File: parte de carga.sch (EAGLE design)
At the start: 28 parts, among them IC1 MCP73831T-2ACI_OT, IC10 741G3157DBVR, IC15 LMV321AIDCKR, IC16 LMV321AIDCKR, IC2 ESP32-S3-WROOM-1-N16R8, IC5 LMV321AIDCKR, IC6 LMV321AIDCKR, IC7 AD8226ARZ, IC8 AD8226ARZ, IC9 LP38692MP-3.3_NOPB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

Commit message: Correcciones del profesor
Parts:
- removed C14: SMDTD03220QA00KS00, SMDTD03220QA00KS00:SMDTD03220QA00KS00
- removed IC6: LMV321AIDCKR, LMV321AIDCKR:LMV321AIDCKR
- removed IC8: AD8226ARZ, AD8226ARZ:AD8226ARZ
- removed R17, R19: (no value), resistor-shunt:BVS
- added R5: (no value), rcl:R-EU_R0805
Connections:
- removed net N$16: IC9.OUT, PS1.EN, PS1.VIN
- removed net N$18: IC8.VOUT
- removed net N$23: IC8.-IN
- removed net N$24: IC7.REF, IC8.REF, PS1.VBIAS
- removed net N$26: IC8.+IN
- removed net N$29: C14.1, IC6.OUT, R19.1
- removed net N$52: C14.2, R19.2
- removed net N$53: IC6.-IN, R17.1
- new net +3V3: IC7.+VS, IC9.OUT, PS1.EN, PS1.VIN
- new net +5V: J1.1
- new net N$10: IC7.RG_1, R5.2
- new net N$12: IC7.RG_2, R5.1
- net GND: now also IC7.-VS; no longer IC6.V-
- net N$22: no longer R17.2
- net VCC: no longer IC6.V+, J1.1
- net VSS: now also IC7.REF, PS1.VBIAS; no longer IC6.+IN
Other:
- moved on the sheet: IC9, PS1

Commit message: cambie resistencias y condensadores
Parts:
- removed C12, C9: SMDTD03220QA00KS00, SMDTD03220QA00KS00:SMDTD03220QA00KS00
- removed R15, R16, R28, R29: (no value), resistor-shunt:BVS
- added C10, C11: 0.1uF, capacitor-wima:C2.5/6
- added C4: 10uF, Capacitor:C-POL_TANTALUM-1206(3216-METRIC)
- added C5, C6, C7: (no value), capacitor-wima:C2.5/6
- added R1, R11, R12: 2k, resistor-shunt:BVS
- added R10: 220, resistor-shunt:BVS
- added R6: 3.2k, resistor-shunt:BVS
- added R7: 1k, resistor-shunt:BVS
- added R8: 10k, resistor-shunt:BVS
- added R9: 450, resistor-shunt:BVS
- C8: value SMDTD03220QA00KS00 -> 10uF; device SMDTD03220QA00KS00:SMDTD03220QA00KS00 -> Capacitor:C-POL_TANTALUM-1206(3216-METRIC)
- R14: value (none) -> 1.6k
- R18: value (none) -> 450
- R5: value (none) -> 50
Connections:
- removed net BATT: SL1.1
- removed net N$22: C9.1, IC5.OUT, R16.1
- removed net N$48: C12.2, R15.2
- removed net N$49: C12.1, R28.1
- new net N$13: C6.2, IC16.+IN, R7.1
- net +BATT: now also C8.+
- net GND: now also C10.2, C11.1, C4.-, C8.-, R1.2, SL1.1
- net N$1: now also R10.1
- net N$2: now also R10.2
- net N$3: now also R1.1
- net N$4: now also C10.1, R11.2
- net N$46: now also R6.2; no longer R29.2
- net N$47: now also C6.1, R6.1, R8.2; no longer R29.1
- net N$5: now also R12.2
- net N$6: now also C5.2; no longer C8.2
- net N$7: now also C7.1, IC5.OUT, R9.1; no longer IC16.-IN, IC16.OUT, R15.1, R18.2
- net N$8: now also IC16.-IN, IC16.OUT, R18.2, R8.1; no longer IC16.+IN
- net N$9: now also C7.2, R9.2; no longer C9.2, R16.2
- net VCC: now also C11.2, C4.+, IC5.V+, R11.1, R12.1
- net VSS: now also R7.2; no longer R28.2
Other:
- moved on the sheet: S1

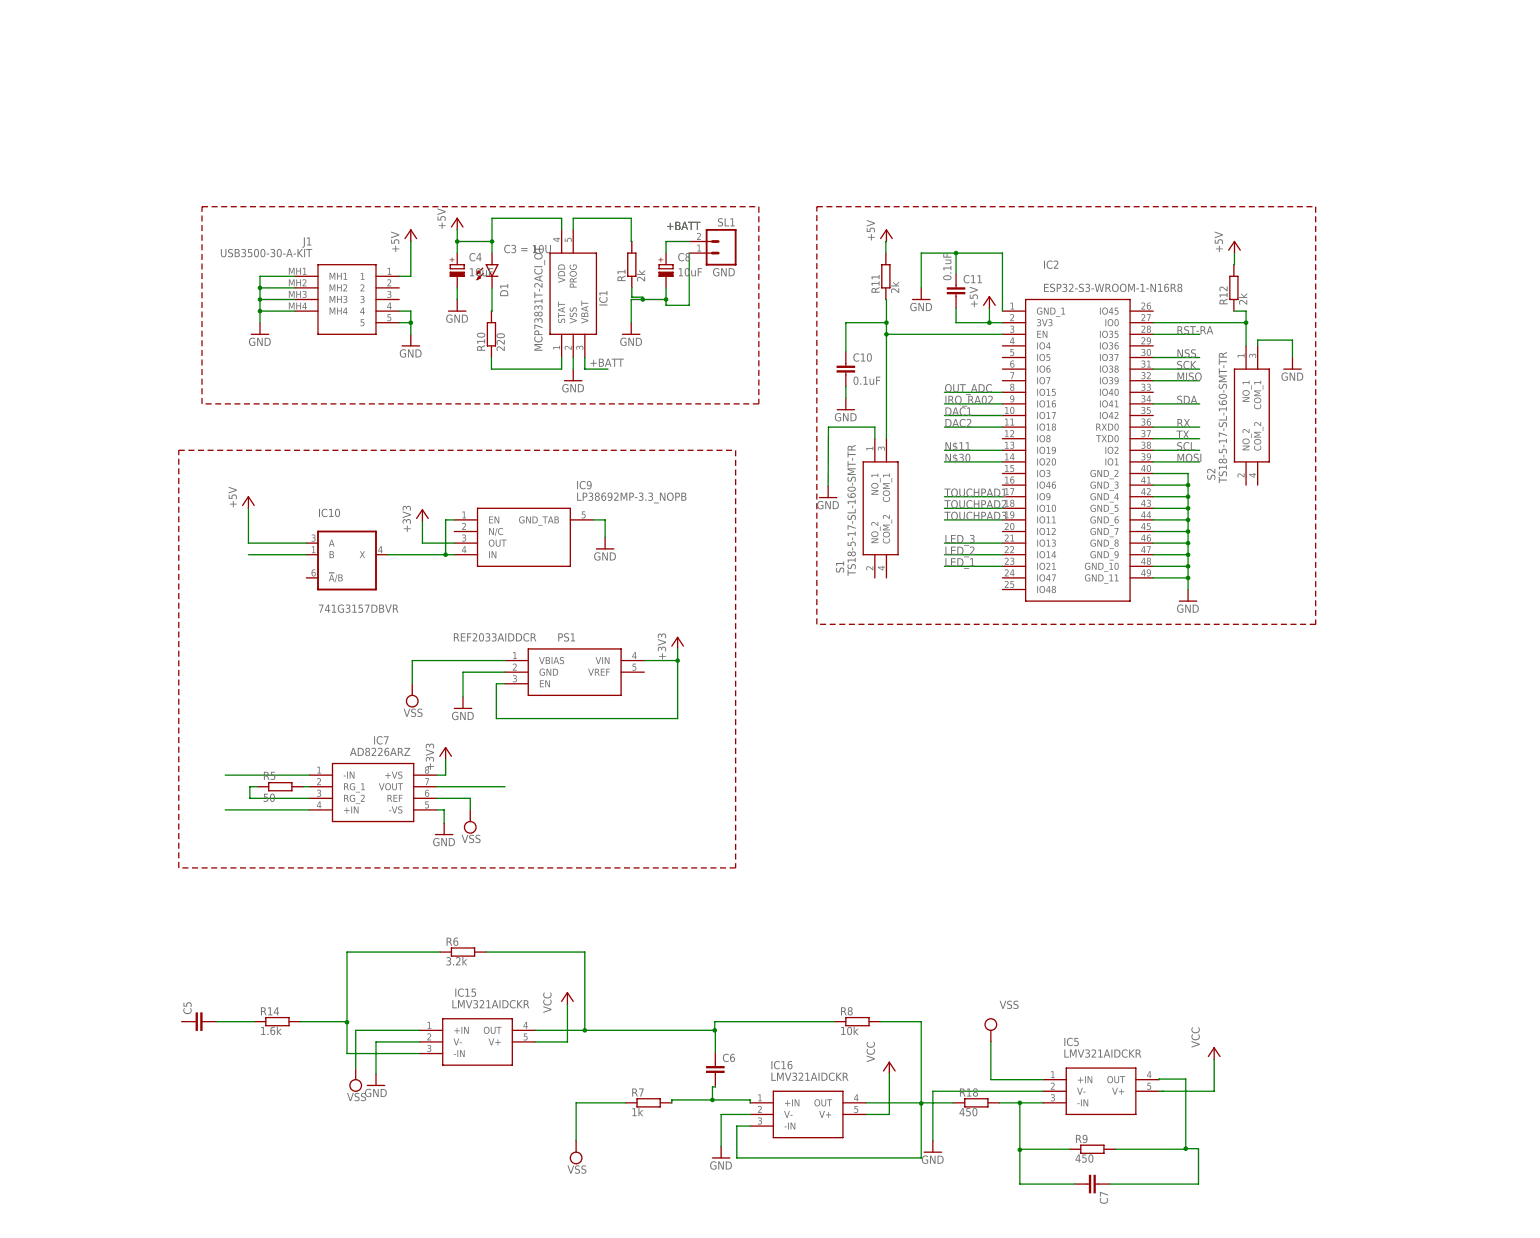
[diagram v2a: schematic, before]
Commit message: Cambie las fuentes y algunos valores a las resistencias
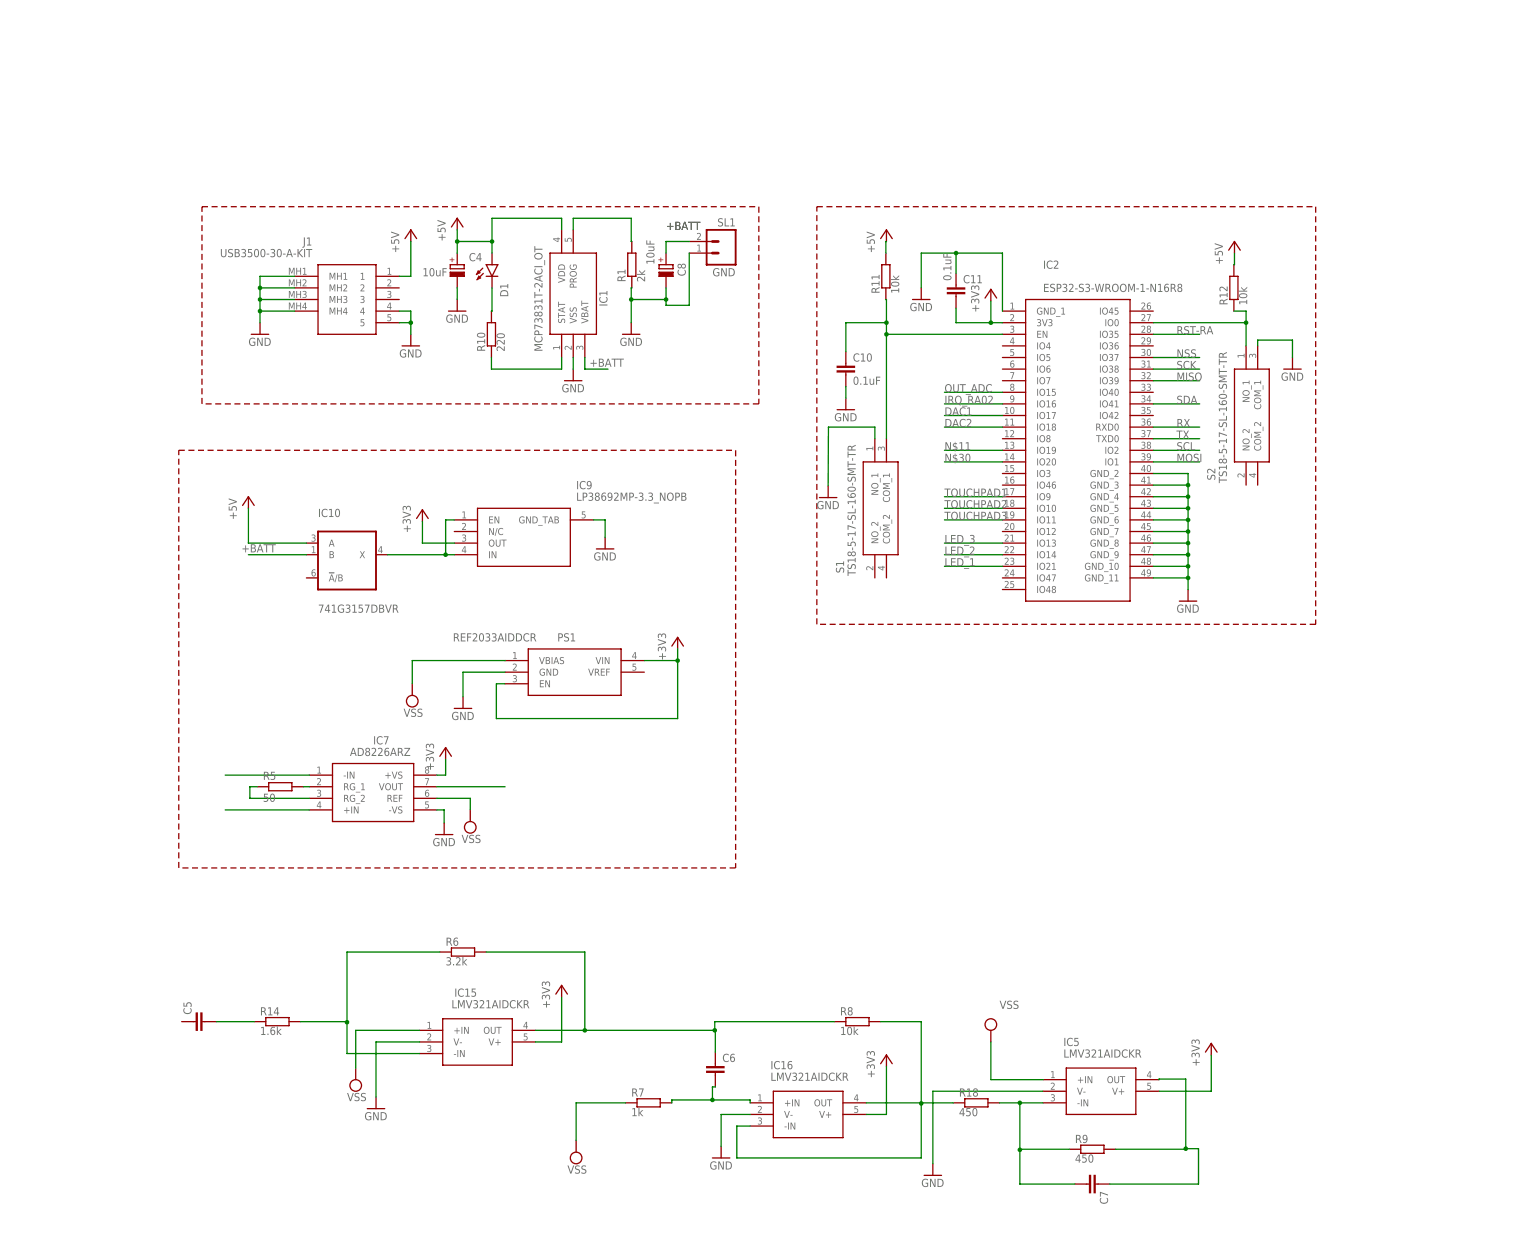
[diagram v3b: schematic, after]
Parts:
- R11, R12: value 2k -> 10k
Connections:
- removed net VCC: C11.2, C4.+, D1.A, IC1.VDD, IC10G$1.A, IC15.V+, IC16.V+, IC2.3V3, IC5.V+, R11.1, R12.1
- net +3V3: now also C11.2, IC15.V+, IC16.V+, IC2.3V3, IC5.V+
- net +5V: now also C4.+, D1.A, IC1.VDD, IC10G$1.A, R11.1, R12.1

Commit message: cambie la escala del esquematico
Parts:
- added R2: (no value), rcl:R-EU_R0805
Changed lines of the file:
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@@
 <setting verticaltext="up"/>
 </settings>
-<grid distance="0.1" unitdist="inch" unit="inch" style="lines" multiple="1" display="no" altdistance="0.01" altunitdist="inch" altunit="inch"/>
+<grid distance="50" unitdist="mil" unit="mil" style="lines" multiple="1" display="no" altdistance="0.01" altunitdist="inch" altunit="inch"/>
 <layers>
-<layer number="1" name="Top" color="4" fill="1" visible="no" active="no"/>
-<layer number="2" name="Route2" color="1" fill="3" visible="no" active="no"/>
-<layer number="3" name="Route3" color="4" fill="3" visible="no" active="no"/>
-<layer number="4" name="Route4" color="1" fill="4" visible="no" active="no"/>
-<layer number="5" name="Route5" color="4" fill="4" visible="no" active="no"/>
-<layer number="6" name="Route6" color="1" fill="8" visible="no" active="no"/>
-<layer number="7" name="Route7" color="4" fill="8" visible="no" active="no"/>
-<layer number="8" name="Route8" color="1" fill="2" visible="no" active="no"/>
-<layer number="9" name="Route9" color="4" fill="2" visible="no" active="no"/>
-<layer number="10" name="Route10" color="1" fill="7" visible="no" active="no"/>
-<layer number="11" name="Route11" color="4" fill="7" visible="no" active="no"/>
-<layer number="12" name="Route12" color="1" fill="5" visible="no" active="no"/>
-<layer number="13" name="Route13" color="4" fill="5" visible="no" active="no"/>
-<layer number="14" name="Route14" color="1" fill="6" visible="no" active="no"/>
-<layer number="15" name="Route15" color="4" fill="6" visible="no" active="no"/>
-<layer number="16" name="Bottom" color="1" fill="1" visible="no" active="no"/>
-<layer number="17" name="Pads" color="2" fill="1" visible="no" active="no"/>
-<layer number="18" name="Vias" color="2" fill="1" visible="no" active="no"/>
-<layer number="19" name="Unrouted" color="6" fill="1" visible="no" active="no"/>
-<layer number="20" name="Dimension" color="15" fill="1" visible="no" active="no"/>
-<layer number="21" name="tPlace" color="7" fill="1" visible="no" active="no"/>
-<layer number="22" name="bPlace" color="7" fill="1" visible="no" active="no"/>
-<layer number="23" name="tOrigins" color="15" fill="1" visible="no" active="no"/>
-<layer number="24" name="bOrigins" color="15" fill="1" visible="no" active="no"/>
-<layer number="25" name="tNames" color="7" fill="1" visible="no" active="no"/>
-<layer number="26" name="bNames" color="7" fill="1" visible="no" active="no"/>
-<layer number="27" name="tValues" color="7" fill="1" visible="no" active="no"/>
-<layer number="28" name="bValues" color="7" fill="1" visible="no" active="no"/>
+<layer number="1" name="Top" color="4" fill="1" visible="yes" active="no"/>
+<layer number="2" name="Route2" color="1" fill="3" visible="yes" active="no"/>
+<layer number="3" name="Route3" color="4" fill="3" visible="yes" active="no"/>
+<layer number="4" name="Route4" color="1" fill="4" visible="yes" active="no"/>
+<layer number="5" name="Route5" color="4" fill="4" visible="yes" active="no"/>
+<layer number="6" name="Route6" color="1" fill="8" visible="yes" active="no"/>
+<layer number="7" name="Route7" color="4" fill="8" visible="yes" active="no"/>
+<layer number="8" name="Route8" color="1" fill="2" visible="yes" active="no"/>
+<layer number="9" name="Route9" color="4" fill="2" visible="yes" active="no"/>
+<layer number="10" name="Route10" color="1" fill="7" visible="yes" active="no"/>
+<layer number="11" name="Route11" color="4" fill="7" visible="yes" active="no"/>
+<layer number="12" name="Route12" color="1" fill="5" visible="yes" active="no"/>
+<layer number="13" name="Route13" color="4" fill="5" visible="yes" active="no"/>
+<layer number="14" name="Route14" color="1" fill="6" visible="yes" active="no"/>
+<layer number="15" name="Route15" color="4" fill="6" visible="yes" active="no"/>
+<layer number="16" name="Bottom" color="1" fill="1" visible="yes" active="no"/>
+<layer number="17" name="Pads" color="2" fill="1" visible="yes" active="no"/>
+<layer number="18" name="Vias" color="2" fill="1" visible="yes" active="no"/>
+<layer number="19" name="Unrouted" color="6" fill="1" visible="yes" active="no"/>
+<layer number="20" name="Dimension" color="24" fill="1" visible="yes" active="no"/>
+<layer number="21" name="tPlace" color="7" fill="1" visible="yes" active="no"/>
+<layer number="22" name="bPlace" color="7" fill="1" visible="yes" active="no"/>
+<layer number="23" name="tOrigins" color="15" fill="1" visible="yes" active="no"/>
+<layer number="24" name="bOrigins" color="15" fill="1" visible="yes" active="no"/>
+<layer number="25" name="tNames" color="7" fill="1" visible="yes" active="no"/>
+<layer number="26" name="bNames" color="7" fill="1" visible="yes" active="no"/>
+<layer number="27" name="tValues" color="7" fill="1" visible="yes" active="no"/>
+<layer number="28" name="bValues" color="7" fill="1" visible="yes" active="no"/>
 <layer number="29" name="tStop" color="7" fill="3" visible="no" active="no"/>
 <layer number="30" name="bStop" color="7" fill="6" visible="no" active="no"/>
@@
 <layer number="35" name="tGlue" color="7" fill="4" visible="no" active="no"/>
 <layer number="36" name="bGlue" color="7" fill="5" visible="no" active="no"/>
-<layer number="37" name="tTest" color="7" fill="1" visible="no" active="no"/>
-<layer number="38" name="bTest" color="7" fill="1" visible="no" active="no"/>
+<layer number="37" name="tTest" color="7" fill="1" visible="yes" active="no"/>
+<layer number="38" name="bTest" color="7" fill="1" visible="yes" active="no"/>
 <layer number="39" name="tKeepout" color="4" fill="11" visible="no" active="no"/>
 <layer number="40" name="bKeepout" color="1" fill="11" visible="no" active="no"/>
@@
 <layer number="44" name="Drills" color="7" fill="1" visible="no" active="no"/>
 <layer number="45" name="Holes" color="7" fill="1" visible="no" active="no"/>
-<layer number="46" name="Milling" color="3" fill="1" visible="no" active="no"/>
-<layer number="47" name="Measures" color="7" fill="1" visible="no" active="no"/>
-<layer number="48" name="Document" color="7" fill="1" visible="no" active="no"/>
-<layer number="49" name="Reference" color="7" fill="1" visible="no" active="no"/>
-<layer number="51" name="tDocu" color="7" fill="1" visible="no" active="no"/>
-<layer number="52" name="bDocu" color="7" fill="1" visible="no" active="no"/>
+<layer number="46" name="Milling" color="3" fill="1" visible="yes" active="no"/>
+<layer number="47" name="Measures" color="7" fill="1" visible="yes" active="no"/>
+<layer number="48" name="Document" color="7" fill="1" visible="yes" active="no"/>
+<layer number="49" name="Reference" color="7" fill="1" visible="yes" active="no"/>
+<layer number="51" name="tDocu" color="7" fill="1" visible="yes" active="no"/>
+<layer number="52" name="bDocu" color="7" fill="1" visible="yes" active="no"/>
 <layer number="88" name="SimResults" color="9" fill="1" visible="yes" active="yes"/>
 <layer number="89" name="SimProbes" color="9" fill="1" visible="yes" active="yes"/>
@@
 <layer number="91" name="Nets" color="2" fill="1" visible="yes" active="yes"/>
 <layer number="92" name="Busses" color="1" fill="1" visible="yes" active="yes"/>
-<layer number="93" name="Pins" color="2" fill="1" visible="no" active="yes"/>
+<layer number="93" name="Pins" color="2" fill="1" visible="yes" active="yes"/>
 <layer number="94" name="Symbols" color="4" fill="1" visible="yes" active="yes"/>
 <layer number="95" name="Names" color="7" fill="1" visible="yes" active="yes"/>
@@
 <part name="P+3" library="supply1" library_urn="urn:adsk.eagle:library:371" deviceset="+5V" device=""/>
 <part name="P+4" library="supply1" library_urn="urn:adsk.eagle:library:371" deviceset="+5V" device=""/>
+<part name="R2" library="rcl" library_urn="urn:adsk.eagle:library:334" deviceset="R-EU_" device="R0805" package3d_urn="urn:adsk.eagle:package:23553/2"/>
 </parts>
 <sheets>
@@
 <attribute name="VALUE" x="-137.16" y="162.56" size="1.778" layer="96" rot="R90"/>
 </instance>
+<instance part="R2" gate="G$1" x="-358.14" y="68.58" smashed="yes">
+<attribute name="NAME" x="-361.95" y="70.0786" size="1.778" layer="95"/>
+<attribute name="VALUE" x="-361.95" y="65.278" size="1.778" layer="96"/>
+</instance>
 </instances>
